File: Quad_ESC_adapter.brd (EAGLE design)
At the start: 65.8 x 39.6 mm, 6 parts

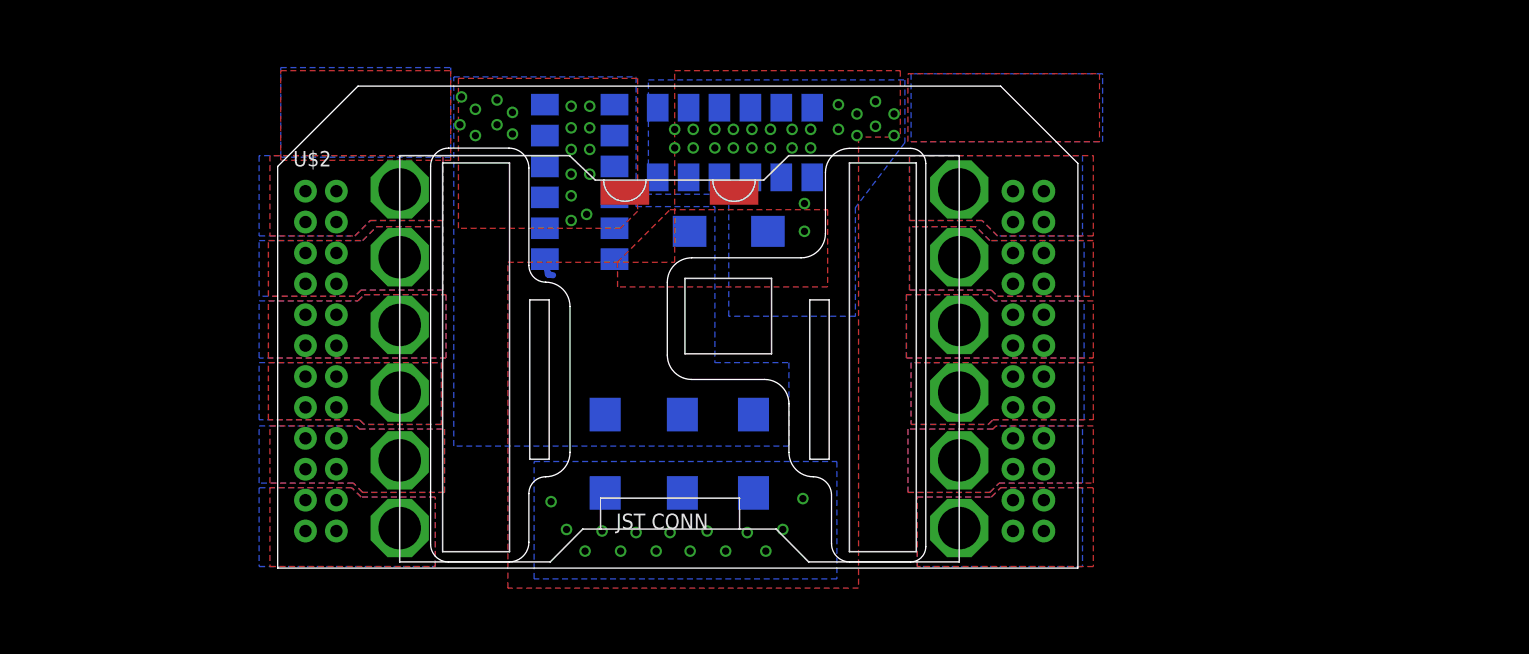
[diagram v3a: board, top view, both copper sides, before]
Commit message: routed wider board
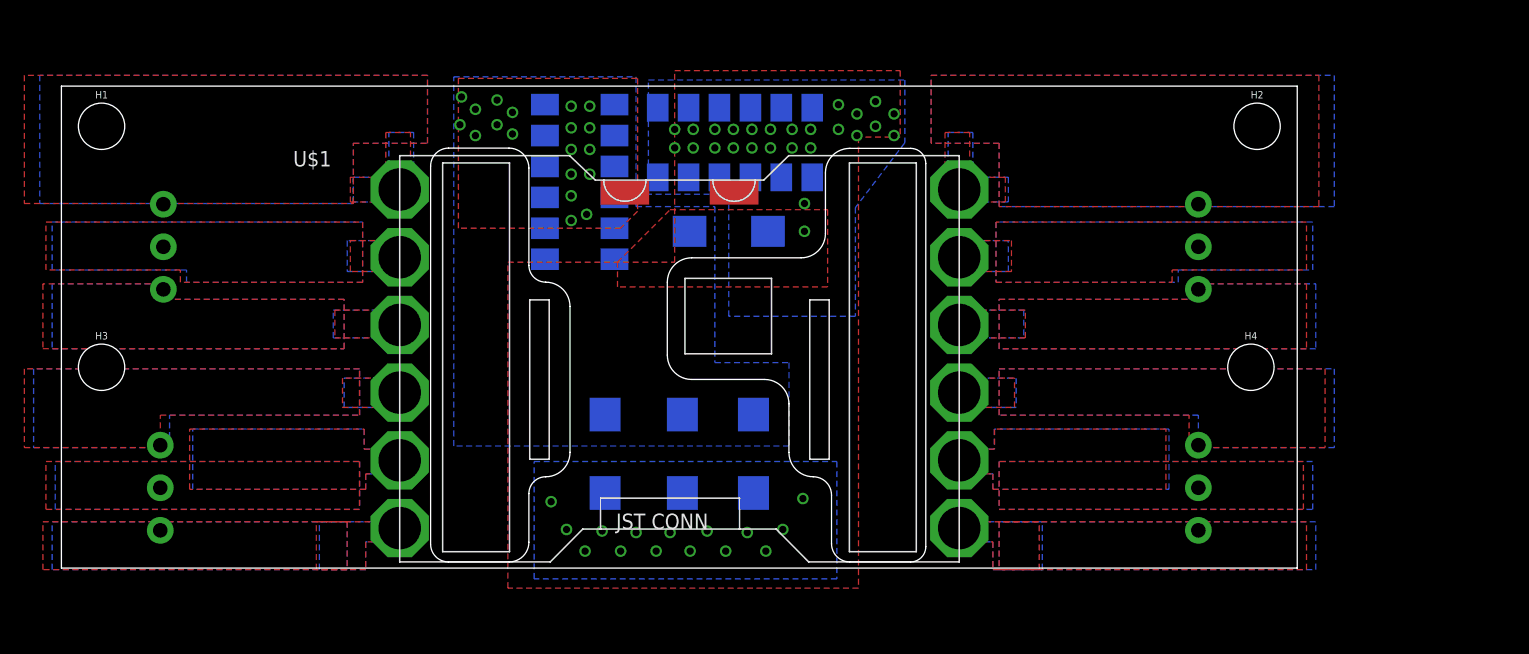
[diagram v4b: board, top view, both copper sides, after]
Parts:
- removed U$2: BACKPLANE_ESC_ADAPTER_ESC, Backplane_ESC_adapter:BACKPLANE_ESC_ADAPTER_ESC
- added H1, H2, H3, H4: 6-32-HOLE, Mounting Holes:6-32-HOLE
- added J1, J2, J3, J4: 284512-3, ThrusterConnector:284512-3
- added U$1: BACKPLANE_ESC_ADAPTER_ESC_PWR, Backplane_ESC_adapter:BACKPLANE_ESC_ADAPTER_ESC_PWR
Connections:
- net 12V: now also U$1.12V@1, U$1.12V@10, U$1.12V@11, U$1.12V@12, U$1.12V@2, U$1.12V@3, U$1.12V@4, U$1.12V@5, U$1.12V@6, U$1.12V@7, U$1.12V@8, U$1.12V@9; no longer U$2.12V@1, U$2.12V@10, U$2.12V@11, U$2.12V@12, U$2.12V@2, U$2.12V@3, U$2.12V@4, U$2.12V@5, U$2.12V@6, U$2.12V@7, U$2.12V@8, U$2.12V@9
- net ESC1_B: now also J1.1; no longer U$2.ESC1_P1@1, U$2.ESC1_P1@2, U$2.ESC1_P1@3, U$2.ESC1_P1@4
- net ESC1_R: now also J1.3; no longer U$2.ESC1_P3@1, U$2.ESC1_P3@2, U$2.ESC1_P3@3, U$2.ESC1_P3@4
- net ESC1_Y: now also J1.2; no longer U$2.ESC1_P2@1, U$2.ESC1_P2@2, U$2.ESC1_P2@3, U$2.ESC1_P2@4
- net ESC2_B: now also J2.1; no longer U$2.ESC2_P1@1, U$2.ESC2_P1@2, U$2.ESC2_P1@3, U$2.ESC2_P1@4
- net ESC2_R: now also J2.3; no longer U$2.ESC2_P3@1, U$2.ESC2_P3@2, U$2.ESC2_P3@3, U$2.ESC2_P3@4
- net ESC2_Y: now also J2.2; no longer U$2.ESC2_P2@1, U$2.ESC2_P2@2, U$2.ESC2_P2@3, U$2.ESC2_P2@4
- net ESC3_B: now also J3.3; no longer U$2.ESC3_P1@1, U$2.ESC3_P1@2, U$2.ESC3_P1@3, U$2.ESC3_P1@4
- net ESC3_R: now also J3.1; no longer U$2.ESC3_P3@1, U$2.ESC3_P3@2, U$2.ESC3_P3@3, U$2.ESC3_P3@4
- net ESC3_Y: now also J3.2; no longer U$2.ESC3_P2@1, U$2.ESC3_P2@2, U$2.ESC3_P2@3, U$2.ESC3_P2@4
- net ESC4_B: now also J4.3; no longer U$2.ESC4_P1@1, U$2.ESC4_P1@2, U$2.ESC4_P1@3, U$2.ESC4_P1@4
- net ESC4_R: now also J4.1; no longer U$2.ESC4_P3@1, U$2.ESC4_P3@2, U$2.ESC4_P3@3, U$2.ESC4_P3@4
- net ESC4_Y: now also J4.2; no longer U$2.ESC4_P2@1, U$2.ESC4_P2@2, U$2.ESC4_P2@3, U$2.ESC4_P2@4
- net GND: now also U$1.GND@1, U$1.GND@10, U$1.GND@11, U$1.GND@12, U$1.GND@2, U$1.GND@3, U$1.GND@4, U$1.GND@5, U$1.GND@6, U$1.GND@7, U$1.GND@8, U$1.GND@9; no longer U$2.GND@1, U$2.GND@10, U$2.GND@11, U$2.GND@12, U$2.GND@2, U$2.GND@3, U$2.GND@4, U$2.GND@5, U$2.GND@6, U$2.GND@7, U$2.GND@8, U$2.GND@9
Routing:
- net GND: track 1.71 -> 0.00 mm
- removed copper zone on layer 1, net FILL_B_L
- removed copper zone on layer 16, net FILL_B_L
- removed copper zone on layer 1, net FILL_B_R
- removed copper zone on layer 16, net FILL_B_R
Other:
- board size 65.8 x 39.6 mm -> 101.6 x 39.6 mm

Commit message: routed with 2x12 block. Basically ready to order
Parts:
- removed U$1: BACKPLANE_ESC_ADAPTER_ESC_PWR, Backplane_ESC_adapter:BACKPLANE_ESC_ADAPTER_ESC_PWR
- added U$2: BACKPLANE_ESC_ADAPTER_PWRESC, Backplane_ESC_adapter:BACKPLANE_ESC_ADAPTER_ESC_PWR
- moved C4 1.52 mm to (38.6, 27.7)
- moved C1 0.51 mm to (26.9, 8.89)
- moved C2 0.51 mm to (33.3, 8.89)
- moved C3 0.51 mm to (39.1, 8.89)
- flipped J1 to the top, turned to 180 degrees
- flipped J2 to the top, turned to 180 degrees
- flipped J3 to the top, turned to 0 degrees
- flipped J4 to the top, turned to 0 degrees
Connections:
- net 12V: now also U$2.12V@1, U$2.12V@10, U$2.12V@11, U$2.12V@12, U$2.12V@2, U$2.12V@3, U$2.12V@4, U$2.12V@5, U$2.12V@6, U$2.12V@7, U$2.12V@8, U$2.12V@9; no longer U$1.12V@1, U$1.12V@10, U$1.12V@11, U$1.12V@12, U$1.12V@2, U$1.12V@3, U$1.12V@4, U$1.12V@5, U$1.12V@6, U$1.12V@7, U$1.12V@8, U$1.12V@9
- net ESC1_B: now also J1.3; no longer J1.1
- net ESC1_R: now also J1.1; no longer J1.3
- net ESC2_B: now also J2.3; no longer J2.1
- net ESC2_R: now also J2.1; no longer J2.3
- net ESC3_B: now also J3.1; no longer J3.3
- net ESC3_R: now also J3.3; no longer J3.1
- net ESC4_B: now also J4.1; no longer J4.3
- net ESC4_R: now also J4.3; no longer J4.1
- net GND: now also U$2.GND@1, U$2.GND@10, U$2.GND@11, U$2.GND@12, U$2.GND@2, U$2.GND@3, U$2.GND@4, U$2.GND@5, U$2.GND@6, U$2.GND@7, U$2.GND@8, U$2.GND@9; no longer U$1.GND@1, U$1.GND@10, U$1.GND@11, U$1.GND@12, U$1.GND@2, U$1.GND@3, U$1.GND@4, U$1.GND@5, U$1.GND@6, U$1.GND@7, U$1.GND@8, U$1.GND@9
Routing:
- net 12V: track 0.00 -> 4.57 mm, vias 41 -> 24
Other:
- board size 101.6 x 39.6 mm -> 101.6 x 41.1 mm
- board text added: "ROV X13 Quad ESC Adapter 1/8/2021 Grant Geyer Scott Hotchkiss"

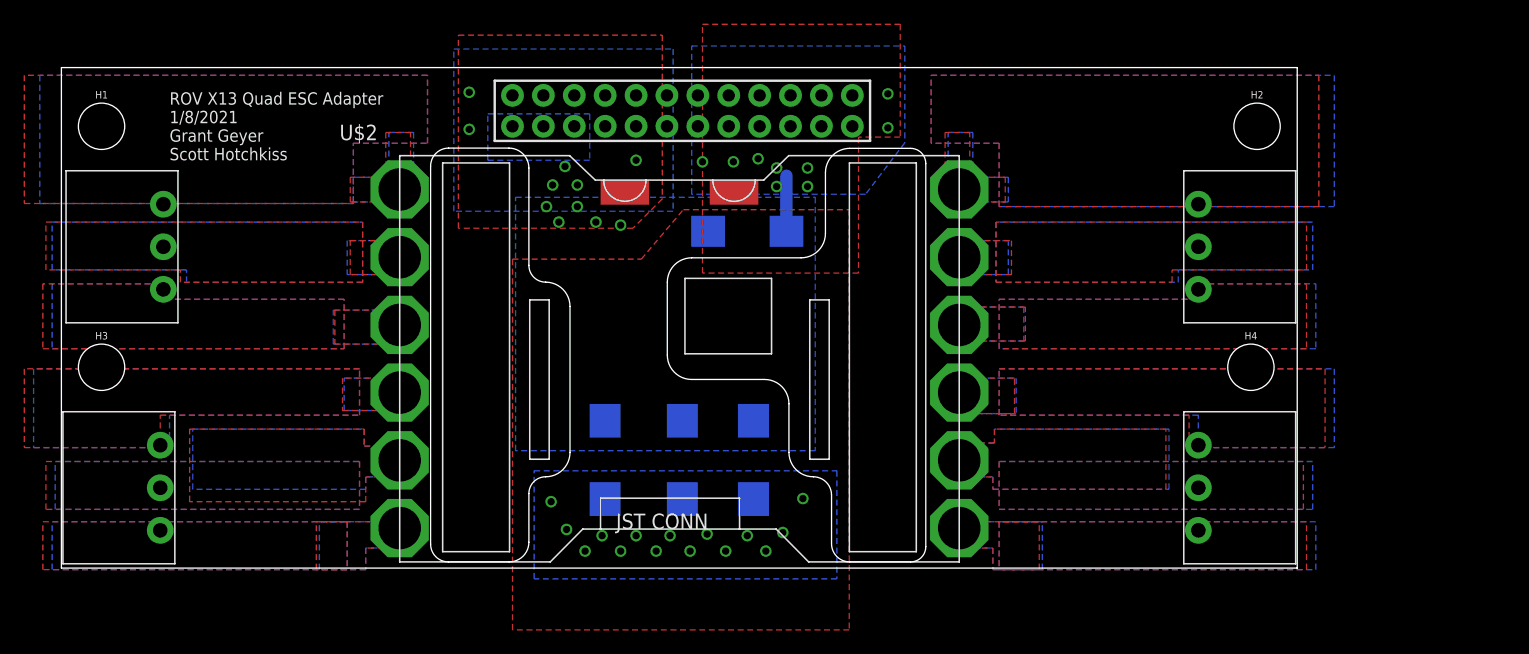
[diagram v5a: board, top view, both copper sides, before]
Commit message: single outline version
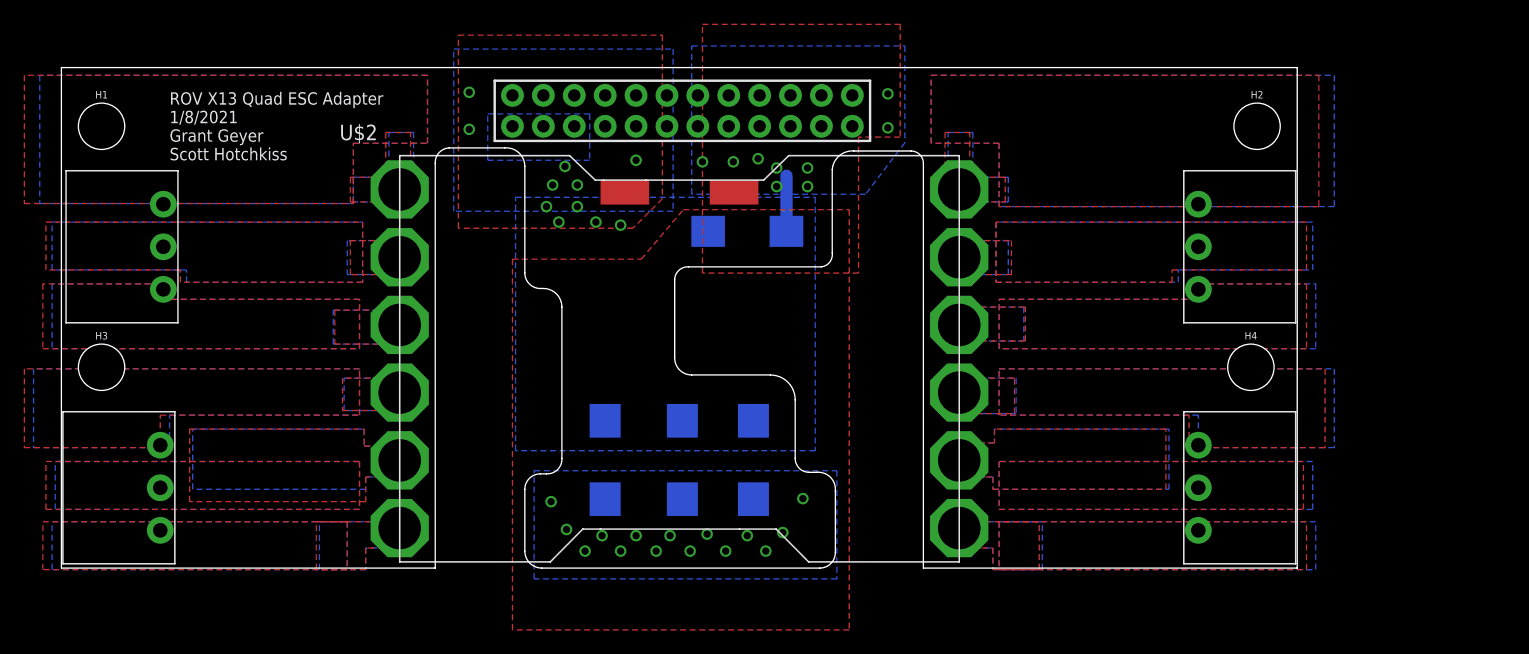
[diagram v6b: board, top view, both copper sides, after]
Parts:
- U$10: value LUMENIER_QUAD -> LUMENIER_QUAD-NO-CUT; device BLHeli_32 45A:LUMENIER_QUAD -> Lumenier ESC:LUMENIER_QUAD-NO-CUT
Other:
- outline, holes or cut-outs redrawn
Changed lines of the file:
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@@
 <setting verticaltext="up"/>
 </settings>
-<grid distance="1" unitdist="mil" unit="mil" style="lines" multiple="1" display="no" altdistance="5" altunitdist="mil" altunit="mil"/>
+<grid distance="5" unitdist="mil" unit="mil" style="lines" multiple="1" display="no" altdistance="5" altunitdist="mil" altunit="mil"/>
 <layers>
 <layer number="1" name="Top" color="4" fill="1" visible="yes" active="yes"/>
@@
 <board>
 <plain>
-<wire x1="-17.78" y1="0" x2="83.82" y2="0" width="0" layer="20"/>
+<wire x1="-17.78" y1="0" x2="12.954" y2="0" width="0" layer="20"/>
+<wire x1="45.847" y1="6.35" x2="45.847" y2="1.27" width="0" layer="20"/>
+<wire x1="20.32" y1="6.477" x2="20.32" y2="1.397" width="0" layer="20"/>
+<wire x1="20.32" y1="1.397" x2="21.717" y2="0" width="0" layer="20" curve="90"/>
+<wire x1="21.717" y1="0" x2="44.577" y2="0" width="0" layer="20"/>
+<wire x1="53.086" y1="0" x2="83.82" y2="0" width="0" layer="20"/>
 <wire x1="83.82" y1="0" x2="83.82" y2="41.148" width="0" layer="20"/>
 <wire x1="83.82" y1="41.148" x2="-17.78" y2="41.148" width="0" layer="20"/>
@@
 Grant Geyer
 Scott Hotchkiss</text>
+<wire x1="14.097" y1="34.544" x2="18.669" y2="34.544" width="0" layer="20"/>
+<wire x1="20.32" y1="33.02" x2="20.32" y2="24.257" width="0" layer="20"/>
+<wire x1="20.32" y1="24.257" x2="21.59" y2="22.987" width="0" layer="20" curve="90"/>
+<wire x1="21.59" y1="22.987" x2="21.844" y2="22.987" width="0" layer="20"/>
+<wire x1="23.368" y1="21.463" x2="23.368" y2="9.017" width="0" layer="20"/>
+<wire x1="22.098" y1="7.747" x2="21.59" y2="7.747" width="0" layer="20"/>
+<wire x1="21.59" y1="7.747" x2="20.32" y2="6.477" width="0" layer="20" curve="90"/>
+<wire x1="14.097" y1="34.544" x2="12.954" y2="33.274" width="0" layer="20" curve="90"/>
+<wire x1="12.954" y1="33.274" x2="12.954" y2="0" width="0" layer="20"/>
+<wire x1="53.086" y1="0" x2="53.086" y2="33.274" width="0" layer="20"/>
+<wire x1="53.086" y1="33.274" x2="52.07" y2="34.29" width="0" layer="20" curve="90"/>
+<wire x1="52.07" y1="34.29" x2="47.371" y2="34.29" width="0" layer="20"/>
+<wire x1="47.371" y1="34.29" x2="45.593" y2="32.766" width="0" layer="20" curve="90"/>
+<wire x1="45.593" y1="32.766" x2="45.593" y2="25.908" width="0" layer="20"/>
+<wire x1="44.704" y1="24.765" x2="33.782" y2="24.765" width="0" layer="20"/>
+<wire x1="33.782" y1="24.765" x2="32.639" y2="23.749" width="0" layer="20" curve="90"/>
+<wire x1="32.639" y1="23.749" x2="32.639" y2="17.272" width="0" layer="20"/>
+<wire x1="32.639" y1="17.272" x2="34.036" y2="15.875" width="0" layer="20" curve="90"/>
+<wire x1="34.036" y1="15.875" x2="40.513" y2="15.875" width="0" layer="20"/>
+<wire x1="42.545" y1="13.843" x2="42.545" y2="9.017" width="0" layer="20"/>
+<wire x1="42.545" y1="9.017" x2="43.688" y2="7.874" width="0" layer="20" curve="90"/>
+<wire x1="43.688" y1="7.874" x2="44.323" y2="7.874" width="0" layer="20"/>
+<wire x1="21.844" y1="22.987" x2="23.368" y2="21.463" width="0" layer="20" curve="-90"/>
+<wire x1="23.368" y1="9.017" x2="22.098" y2="7.747" width="0" layer="20" curve="-96.025575"/>
+<wire x1="45.847" y1="1.27" x2="44.577" y2="0" width="0" layer="20" curve="-90"/>
+<wire x1="44.323" y1="7.874" x2="45.847" y2="6.35" width="0" layer="20" curve="-100.388858"/>
+<wire x1="40.513" y1="15.875" x2="42.545" y2="13.843" width="0" layer="20" curve="-90"/>
+<wire x1="45.593" y1="25.908" x2="44.704" y2="24.765" width="0" layer="20" curve="-90"/>
+<wire x1="18.669" y1="34.544" x2="20.32" y2="33.02" width="0" layer="20" curve="-94.763642"/>
 </plain>
 <attributes>
@@
 </autorouter>
 <elements>
-<element name="U$10" library="BLHeli_32 45A" package="LUMENIER_QUAD" package3d_urn="urn:adsk.eagle:package:24294694/3" value="LUMENIER_QUAD" x="10.033" y="0.508" smashed="yes"/>
+<element name="U$10" library="Lumenier ESC" package="LUMENIER_QUAD-NO-CUT" package3d_urn="urn:adsk.eagle:package:24294694/3" value="LUMENIER_QUAD-NO-CUT" x="10.033" y="0.508" smashed="yes"/>
 <element name="C1" library="Tantalum Cap 150 uF - Kemet 2917 T491" package="2917(7343-31-METRIC)" package3d_urn="urn:adsk.eagle:package:25131320/3" value="150uF" x="26.924" y="8.89" smashed="yes" rot="MR90">
 <attribute name="NAME" x="29.464" y="8.89" size="1.27" layer="26" rot="MR90" align="bottom-center"/>
@@
 <polygon width="1.016" layer="16" isolate="0.3048">
 <vertex x="-18.542" y="18.034"/>
-<vertex x="5.461" y="18.034"/>
-<vertex x="5.461" y="22.098"/>
+<vertex x="6.731" y="18.034"/>
+<vertex x="6.731" y="22.098"/>
 <vertex x="-8.89" y="22.098"/>
 <vertex x="-8.89" y="23.368"/>
@@
 <polygon width="1.016" layer="1" isolate="0.3048">
 <vertex x="-19.304" y="18.034"/>
-<vertex x="5.461" y="18.034"/>
-<vertex x="5.461" y="22.098"/>
+<vertex x="6.731" y="18.034"/>
+<vertex x="6.731" y="22.098"/>
 <vertex x="-9.652" y="22.098"/>
 <vertex x="-9.652" y="23.368"/>
